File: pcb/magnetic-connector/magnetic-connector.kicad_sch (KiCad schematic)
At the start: 8 parts

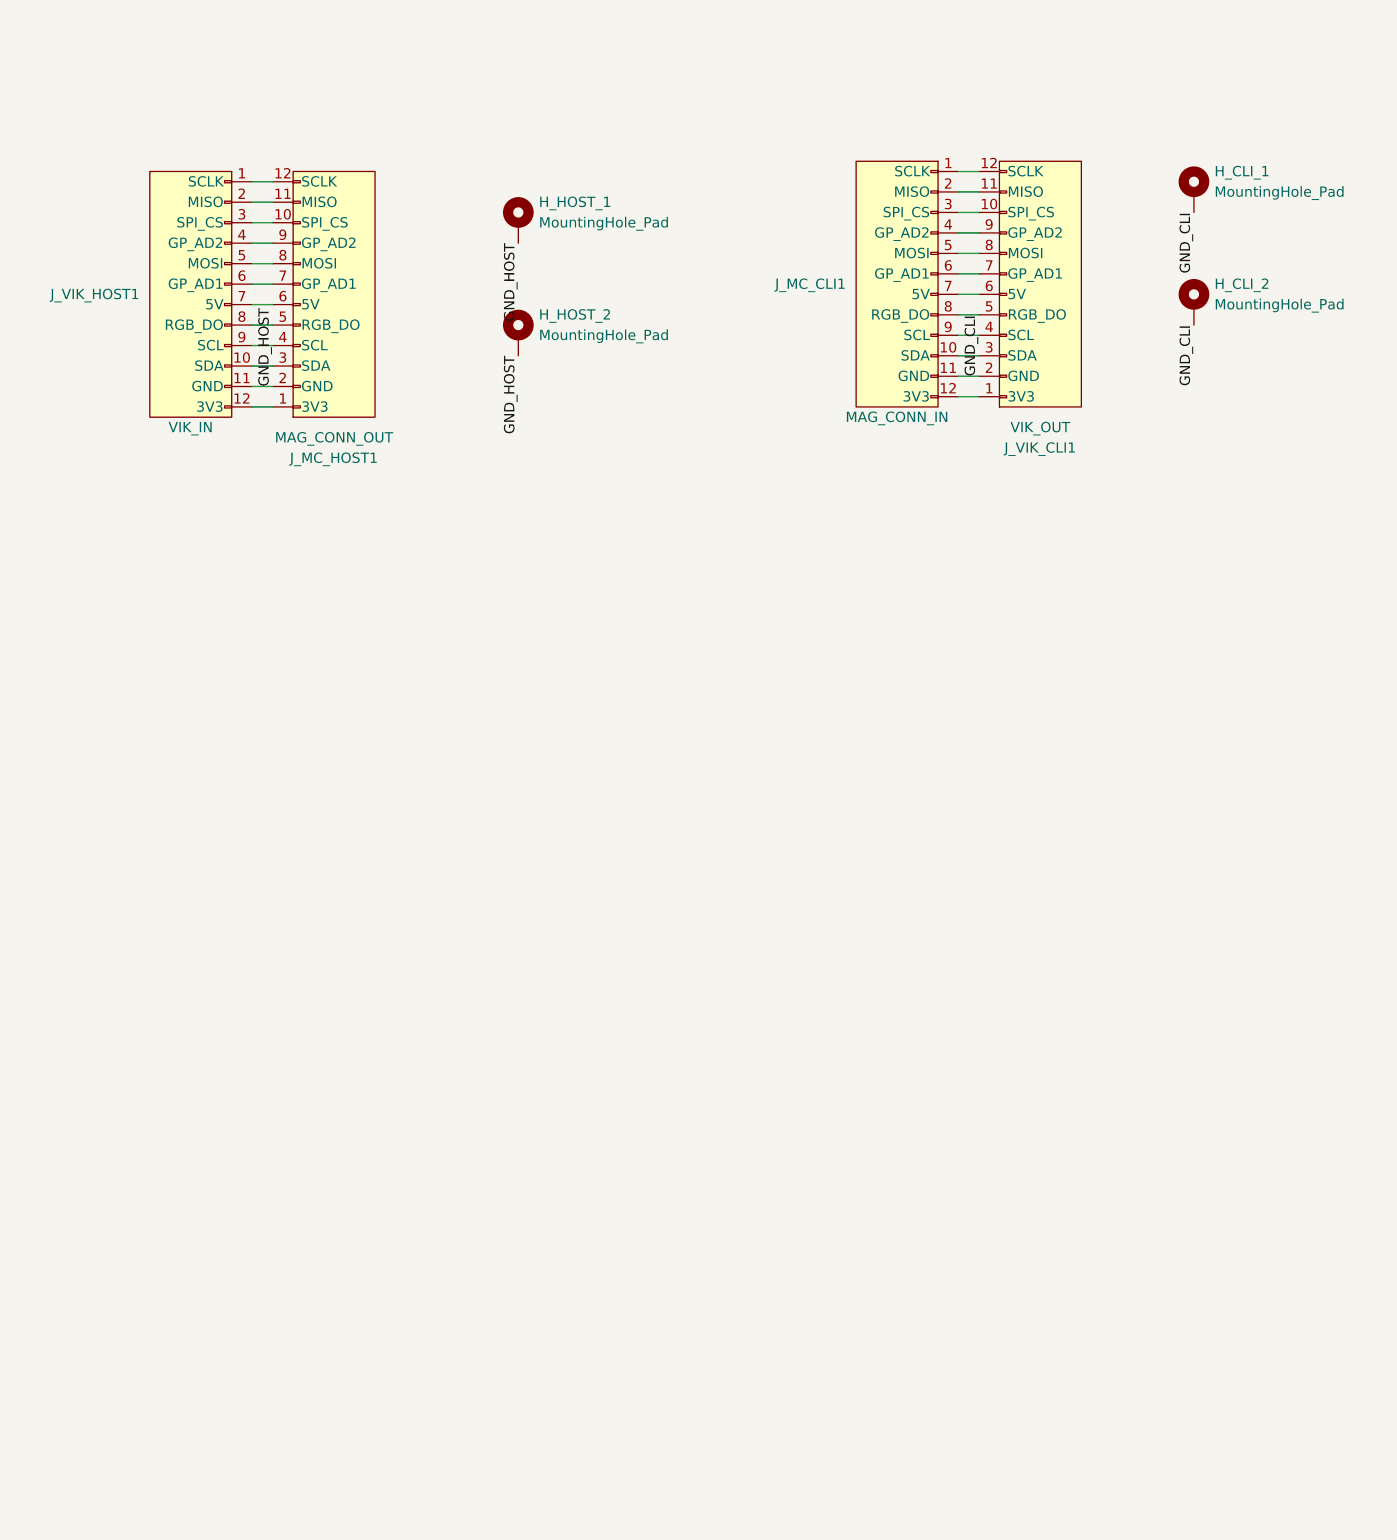
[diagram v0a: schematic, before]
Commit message: Add ESD protection to magnetic connector module.
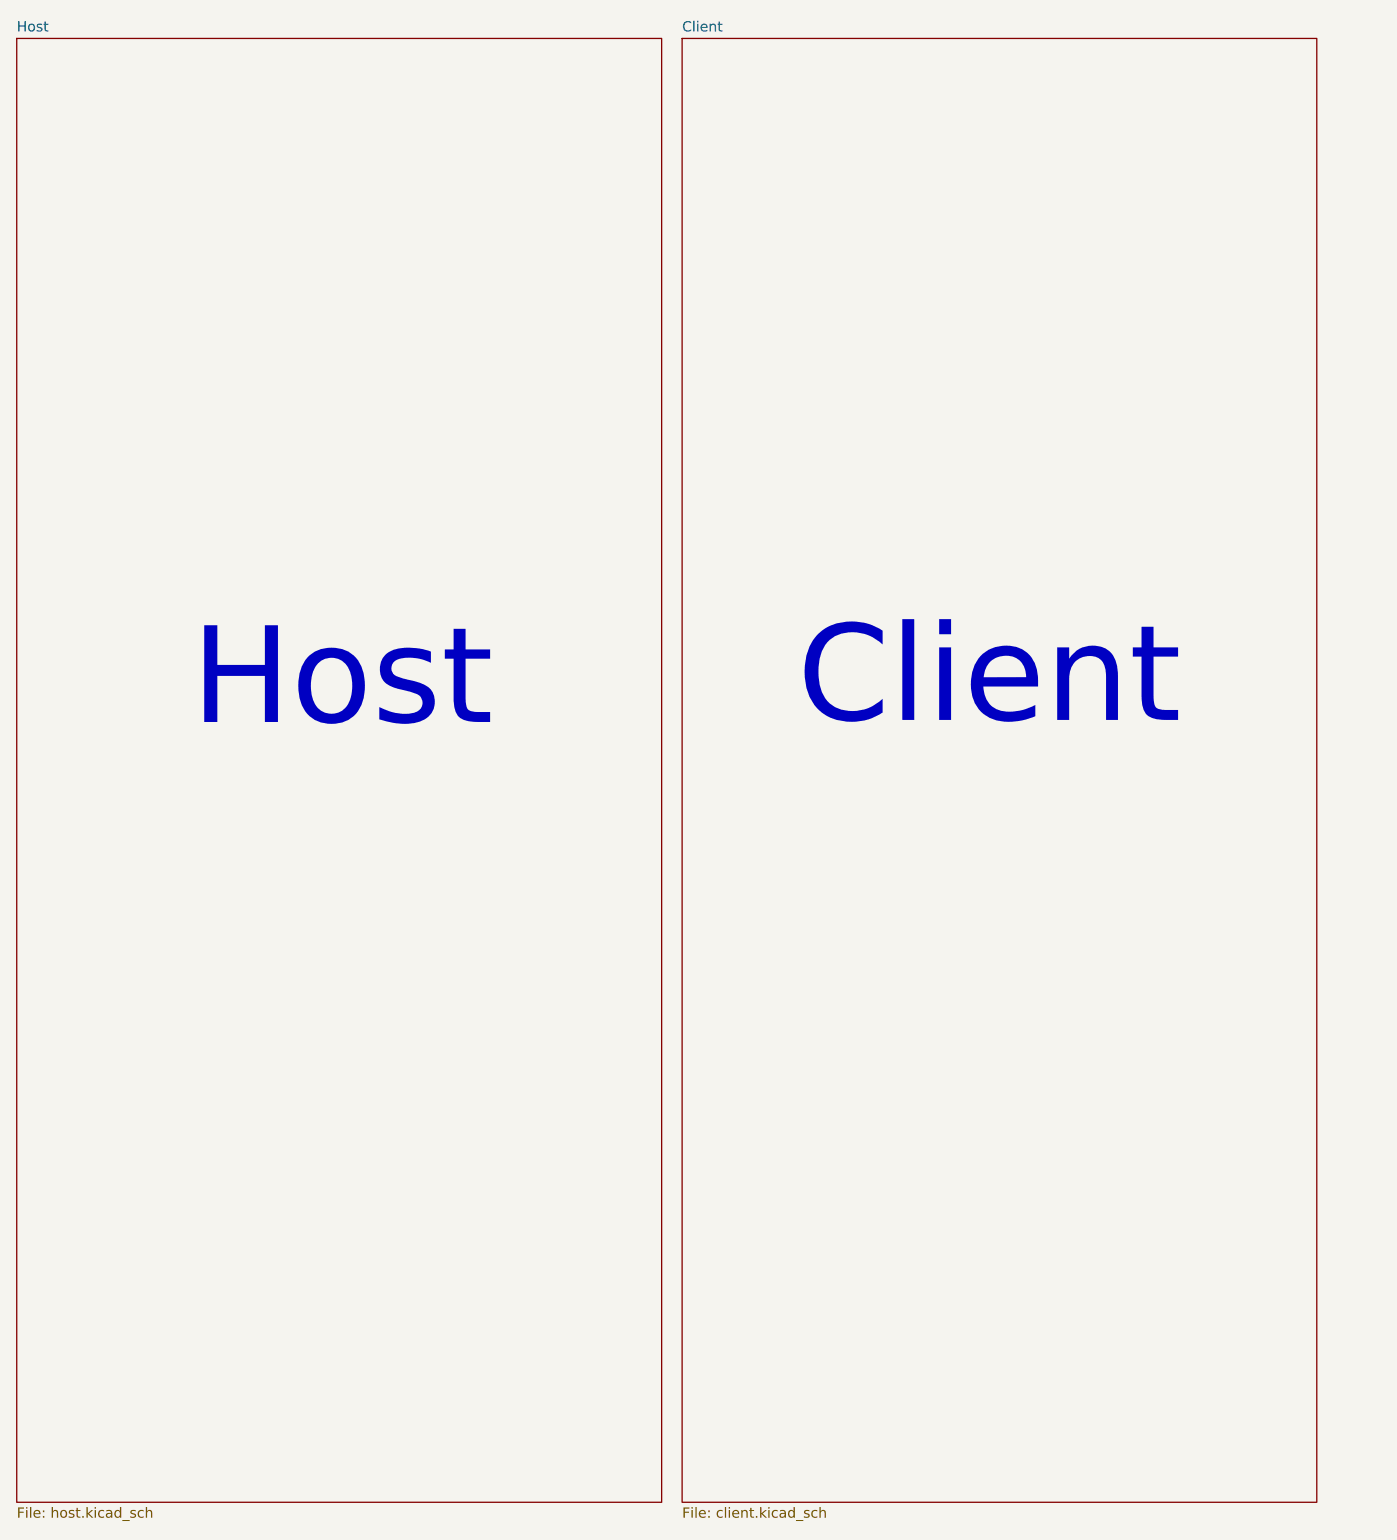
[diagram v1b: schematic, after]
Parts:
- removed H_CLI_1, H_CLI_2, H_HOST_1, H_HOST_2: MountingHole_Pad, MountingHole:MountingHole_2.2mm_M2_Pad, symbol Mechanical:MountingHole_Pad
- removed J_MC_CLI1: MAG_CONN_IN, magnetic-connector:vik-module-throughole-2.2mm, symbol vik:vik-module-connector
- removed J_MC_HOST1: MAG_CONN_OUT, magnetic-connector:vik-keyboard-throughole-2.2mm, symbol vik:vik-keyboard-connector
- removed J_VIK_CLI1: VIK_OUT, vik:vik-keyboard-connector-vertical, symbol vik:vik-keyboard-connector
- removed J_VIK_HOST1: VIK_IN, vik:vik-module-connector-vertical, symbol vik:vik-module-connector
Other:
- added sheet Client (client.kicad_sch)
- added sheet Host (host.kicad_sch)
- note added: "Client"
- note added: "Host"
